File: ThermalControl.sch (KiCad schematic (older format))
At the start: 19 parts, among them U501 ADA4528-2ACPZ-RL, U502 ADA4528-2ACPZ-RL

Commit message: replaced thermistor w/ butterfly
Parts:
- removed TH501: Thermistor, symbol Device:Thermistor
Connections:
- net labels added: Butterfly_Thermistor
- wire segments 69 -> 71
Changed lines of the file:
@@
 U 1 1 60C2FA14
 P 5600 3900
-F 0 "R504" V 5700 3700 50  0000 L CNN
-F 1 "10k" V 5700 3950 50  0000 L CNN
+F 0 "R504" V 5700 3750 50  0000 L CNN
+F 1 "10k" V 5700 3900 50  0000 L CNN
 F 2 "Resistor_SMD:R_0603_1608Metric" V 5530 3900 50  0001 C CNN
 F 3 "~" H 5600 3900 50  0001 C CNN
@@
 $EndComp
 $Comp
-L Device:Thermistor TH501
-U 1 1 60C34A4A
-P 3700 4950
-F 0 "TH501" H 3805 4996 50  0000 L CNN
-F 1 "Thermistor" H 3805 4905 50  0000 L CNN
-F 2 "" H 3700 4950 50  0001 C CNN
-F 3 "~" H 3700 4950 50  0001 C CNN
-	1    3700 4950
-	1    0    0    -1
-$EndComp
-$Comp
 L Device:C C501
 U 1 1 60C35080
@@
 	4800 4750 4450 4750
 $Comp
-L power:GND #PWR0501
-U 1 1 60C40715
-P 3700 5150
-F 0 "#PWR0501" H 3700 4900 50  0001 C CNN
-F 1 "GND" H 3705 4977 50  0000 C CNN
-F 2 "" H 3700 5150 50  0001 C CNN
-F 3 "" H 3700 5150 50  0001 C CNN
-	1    3700 5150
-	1    0    0    -1
-$EndComp
-$Comp
 L power:GND #PWR0503
 U 1 1 60C40C53
@@
 	1    0    0    -1
 $EndComp
-Connection ~ 3700 4750
-Wire Wire Line
-	3700 4750 3400 4750
 Connection ~ 4450 4750
 Wire Wire Line
@@
 	4250 4750 4250 6150
 Connection ~ 4250 4750
-Wire Wire Line
-	4250 4750 3700 4750
 Wire Wire Line
 	2850 4750 2850 5700
@@
 Text Label 2400 4750 0    50   ~ 0
 Reference_2.5_AC
+Wire Wire Line
+	3400 4750 3800 4750
+Wire Wire Line
+	3800 4750 3800 4200
+Wire Wire Line
+	3800 4200 2200 4200
+Connection ~ 3800 4750
+Wire Wire Line
+	3800 4750 4250 4750
+Text Label 2200 4200 0    50   ~ 0
+Butterfly_Thermistor
 $EndSCHEMATC

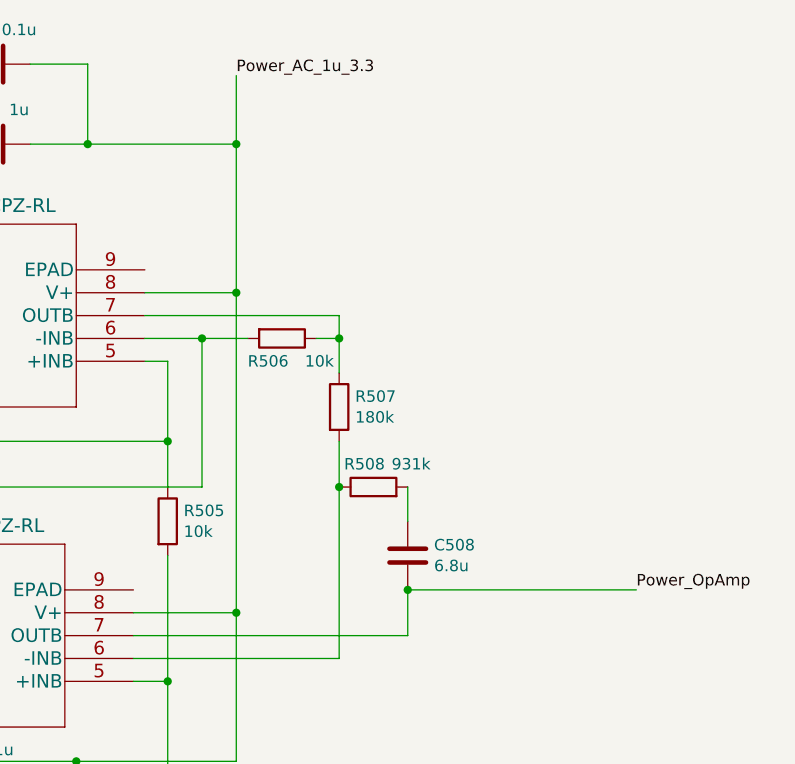
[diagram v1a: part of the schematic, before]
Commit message: added more ports
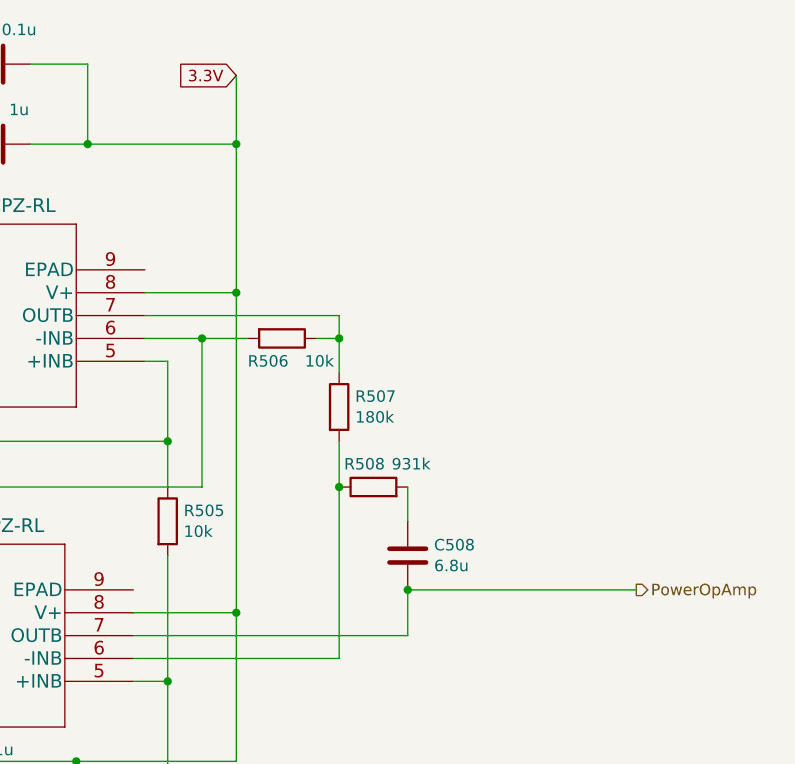
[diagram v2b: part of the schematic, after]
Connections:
- net Power_AC_1u_3.3 renamed 3.3V
- net Power_OpAmp renamed PowerOpAmp
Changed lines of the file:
@@
 Wire Wire Line
 	6150 5300 6850 5300
-Text Label 8600 4550 0    50   ~ 0
-Power_OpAmp
-Text Label 6850 2300 0    50   ~ 0
-Power_AC_1u_3.3
 Wire Wire Line
 	3550 2650 4100 2650
@@
 Text Label 2200 4200 0    50   ~ 0
 Butterfly_Thermistor
+Text GLabel 6850 2300 0    50   Input ~ 0
+3.3V
+Text HLabel 8600 4550 2    50   Output ~ 0
+PowerOpAmp
 $EndSCHEMATC

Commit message: pushing all changes and ports
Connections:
- net Reference_2.5_AC renamed REFERENCE_2.5V
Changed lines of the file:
@@
 Text Label 4250 6150 0    50   ~ 0
 AtoD_Input
-Text Label 2400 4750 0    50   ~ 0
-Reference_2.5_AC
 Wire Wire Line
 	3400 4750 3800 4750
@@
 Text HLabel 8600 4550 2    50   Output ~ 0
 PowerOpAmp
+Text GLabel 2400 4750 0    50   Input ~ 0
+REFERENCE_2.5V
 $EndSCHEMATC

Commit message: keep on adding global labels
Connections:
- net AtoD_Input renamed Therm_to_AtoD
- net Setpoint renamed DtoA_Output_(Setpoint)
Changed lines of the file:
@@
 Wire Wire Line
 	3100 4750 2850 4750
-Wire Wire Line
-	4250 4750 4250 6150
 Connection ~ 4250 4750
 Wire Wire Line
@@
 Wire Wire Line
 	3550 2650 4100 2650
-Text Label 3550 2650 0    50   ~ 0
-Setpoint
-Text Label 4250 6150 0    50   ~ 0
-AtoD_Input
 Wire Wire Line
 	3400 4750 3800 4750
@@
 Text GLabel 2400 4750 0    50   Input ~ 0
 REFERENCE_2.5V
+Text GLabel 3550 2650 0    50   Input ~ 0
+DtoA_Output_(Setpoint)
+Text GLabel 4250 6550 2    50   Input ~ 0
+Therm_to_AtoD
+Wire Wire Line
+	4250 4750 4250 6550
 $EndSCHEMATC

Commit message: did current control
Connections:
- net PowerOpAmp renamed Thermal_Control_to_Power_OpAmps
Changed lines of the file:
@@
 Text GLabel 6850 2300 0    50   Input ~ 0
 3.3V
-Text HLabel 8600 4550 2    50   Output ~ 0
-PowerOpAmp
 Text GLabel 2400 4750 0    50   Input ~ 0
 REFERENCE_2.5V
@@
 Wire Wire Line
 	4250 4750 4250 6550
+Text GLabel 8600 4550 2    50   Output ~ 0
+Thermal_Control_to_Power_OpAmps
 $EndSCHEMATC

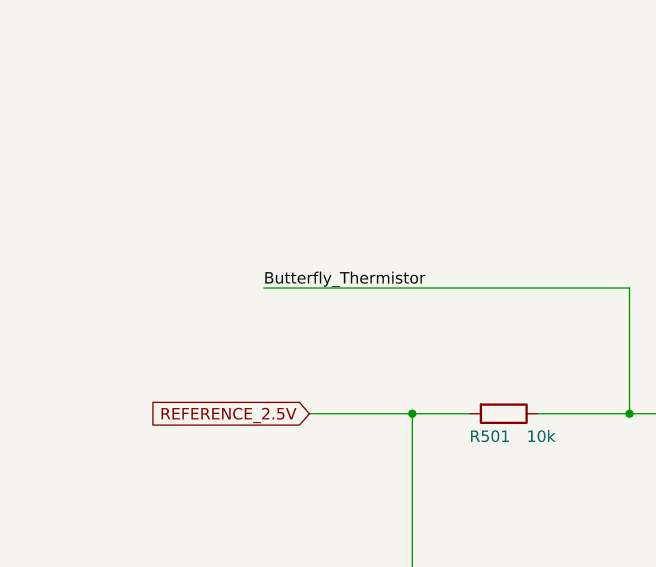
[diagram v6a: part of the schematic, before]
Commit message: made butterfly a global label, connected SDA & SCL
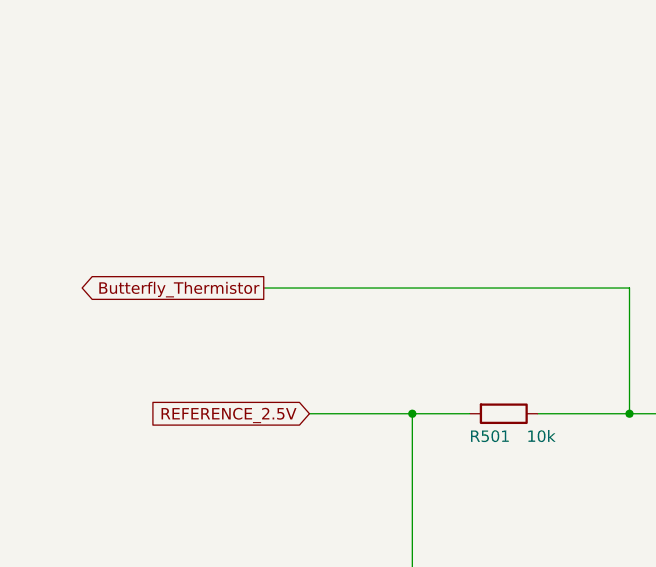
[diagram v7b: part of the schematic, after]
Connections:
- net Therm_to_AtoD renamed Butterfly_Thermistor
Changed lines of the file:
@@
 Wire Wire Line
 	3800 4750 4250 4750
-Text Label 2200 4200 0    50   ~ 0
-Butterfly_Thermistor
 Text GLabel 6850 2300 0    50   Input ~ 0
 3.3V
@@
 Text GLabel 8600 4550 2    50   Output ~ 0
 Thermal_Control_to_Power_OpAmps
+Text GLabel 2200 4200 0    50   Output ~ 0
+Butterfly_Thermistor
 $EndSCHEMATC
